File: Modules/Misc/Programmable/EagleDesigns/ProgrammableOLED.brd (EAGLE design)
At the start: 100 x 80 mm, 12 parts, among them U2 ATMEGA328P_TQFP

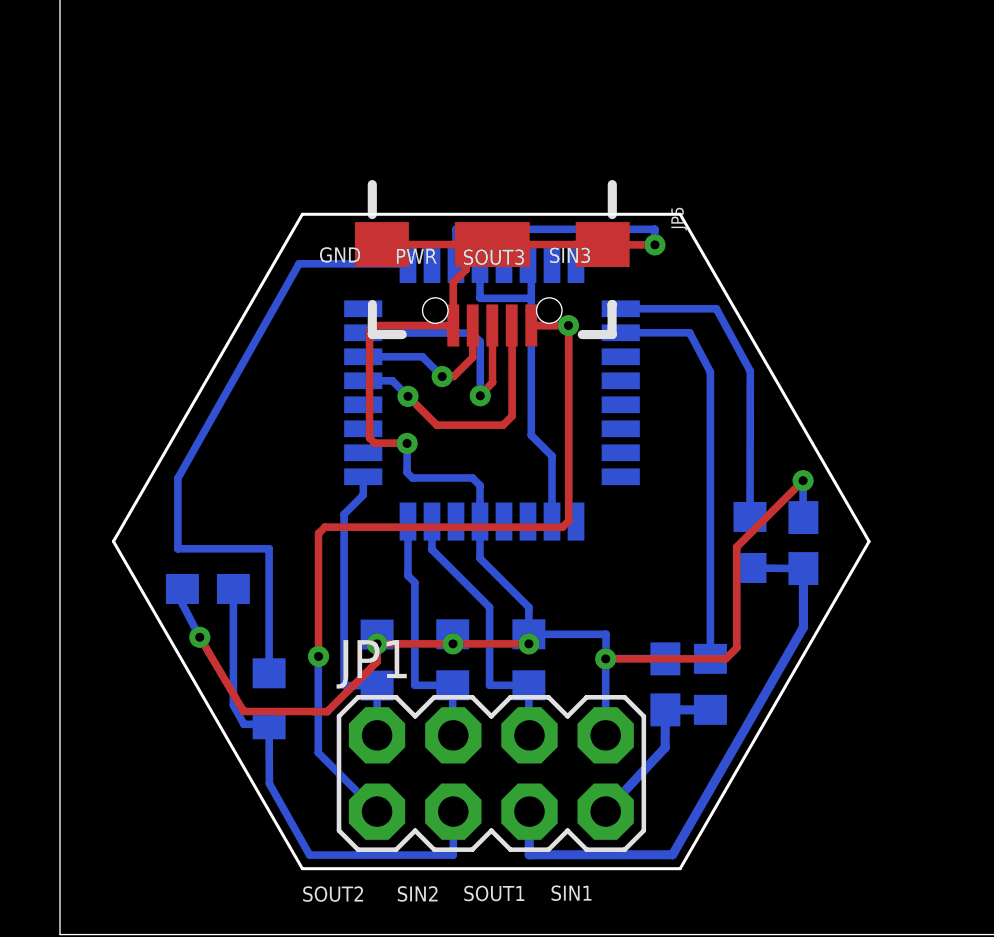
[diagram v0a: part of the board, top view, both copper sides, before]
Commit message: moved MicroUSB more into the hexagon, removed holes for MicroUSB & OLED
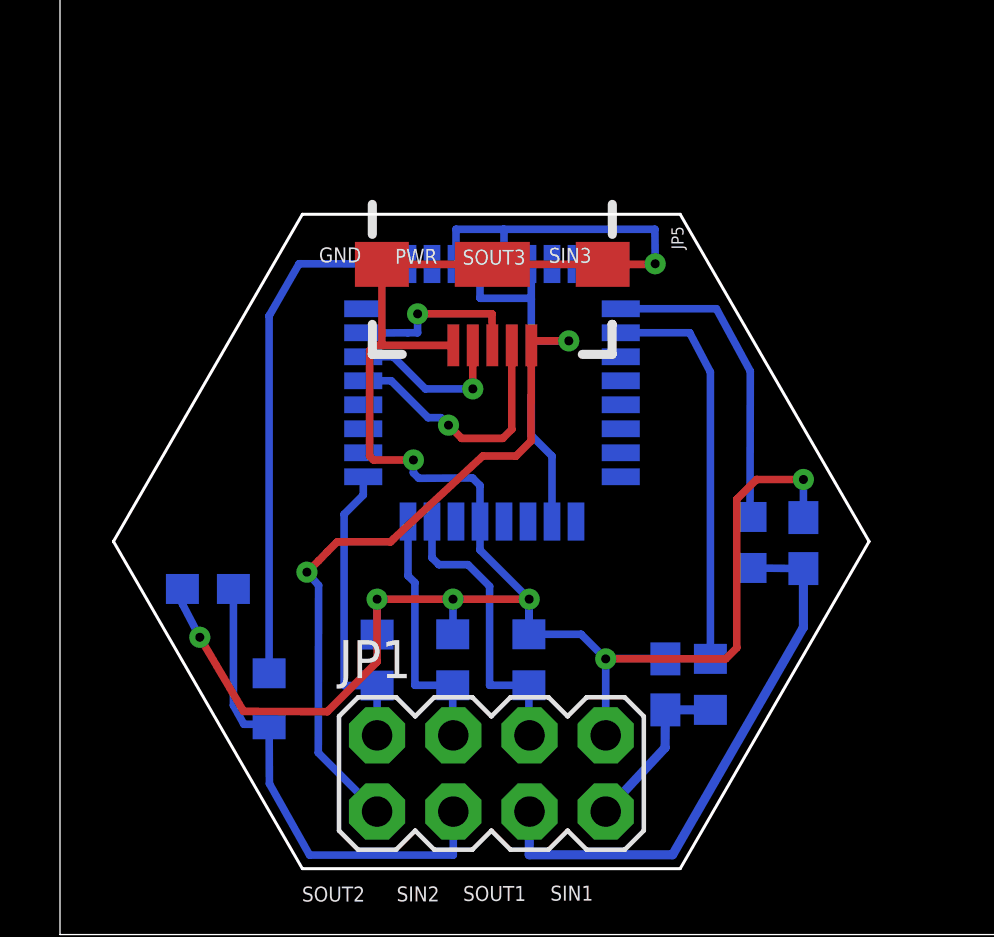
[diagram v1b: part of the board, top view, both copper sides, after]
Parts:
- moved JP5 0.66 mm to (14.4, 22.3)
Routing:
- net GND: track 75.1 -> 79.2 mm
- net OUT1: track 21.4 -> 17.5 mm
- net VCC: track 39.5 -> 35.9 mm
- net TX: track 8.37 -> 6.01 mm
- net SIN1: track 9.24 -> 9.81 mm
